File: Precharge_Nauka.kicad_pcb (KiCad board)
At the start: 4 copper layers, 100.8 x 101.4 mm, 238 parts, among them J1 Conn_02x02_Top_Bottom, J2 Conn_01x01, J3 Conn_01x01, J4 Conn_01x01, Q1 2N7002, Q2 C2M0280120D, Q3 C2M0280120D, Q4 C2M0280120D, Q5 C2M0280120D, U1 LM2903, U2 LMV321IDBVR, U3 74LVC1G08, U4 LMV321IDBVR

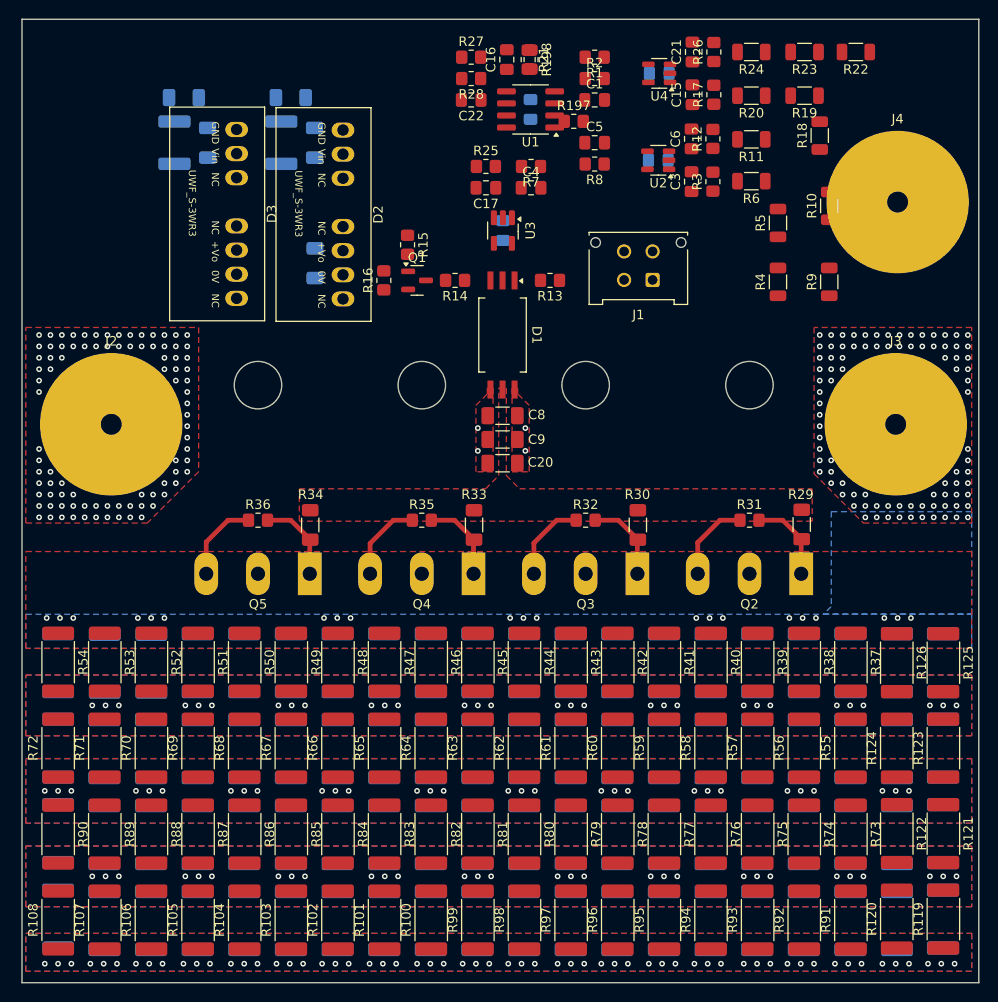
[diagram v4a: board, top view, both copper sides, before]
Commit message: VER1.0: увеличил фильтры компаратора, изменил схему предзарядных резисторов
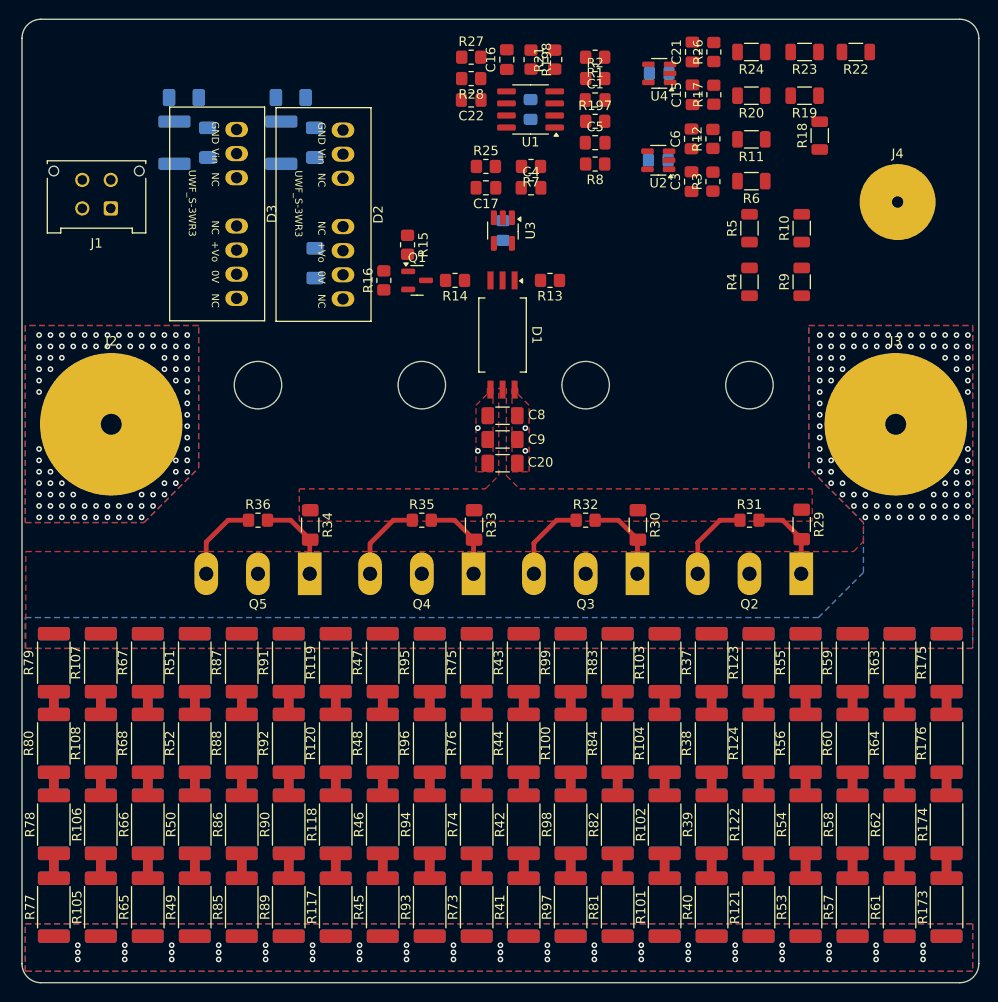
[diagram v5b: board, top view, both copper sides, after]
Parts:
- C16, C17, C4, C5: value 100n -> 1u
- J4: footprint Connector_Power:SMD_15mm -> Connector_Power:SMD_8mm
- R100, R101, R102, R103, R104, R105, R106, R107, R108, R109, R110, R111, R112, R113, R114, R115, R116, R119, R120, R121, R122, R123, R124, R127, R128, R129, R130, R131, R132, R133, R134, R135, R136, R137, R138, R139, R140, R141, R142, R143, R144, R145, R146, R147, R148, R149, R150, R151, R152, R153, R154, R155, R156, R157, R158, R159, R160, R161, R162, R163, R164, R165, R166, R167, R168, R169, R170, R171, R172, R177, R178, R179, R180, R181, R182, R183, R184, R185, R186, R187, R188, R189, R190, R191, R192, R193, R194, R195, R196, R37, R38, R39, R40, R41, R42, R43, R44, R45, R46, R47, R48, R49, R50, R51, R52, R53, R54, R55, R56, R57, R58, R59, R60, R61, R62, R63, R64, R65, R66, R67, R68, R73, R74, R75, R76, R77, R78, R79, R80, R81, R82, R83, R84, R85, R86, R87, R88, R89, R90, R91, R92, R93, R94, R95, R96, R97, R98, R99: value 15 -> 8.2k
- R117, R118, R173, R174, R175, R176: value 15 -> 8.2k; moved to F.Cu
- R125, R126, R69, R70, R71, R72: value 15 -> 8.2k; moved to B.Cu
- R197, R198: value 10k -> 100k
- R21, R8: value 120 -> 1k
- R25, R7: value 120 -> 10k
- U1: value LM2903 -> TS3702IDT
- moved R163 89.2 mm to (138.8, 189.5)
- moved R72 88.6 mm to (227.8, 198.0)
- moved R181 87.7 mm to (143.7, 215.2)
- moved R71 84.2 mm to (227.8, 189.5)
- moved R164 83.9 mm to (138.8, 198.0)
- moved R144 81.0 mm to (222.9, 198.0)
- moved R115 80.7 mm to (217.9, 189.5), turned to 90 degrees
- moved R182 80.7 mm to (143.7, 206.5)
- moved R54 80.5 mm to (217.9, 206.6)
- moved R113 80.5 mm to (217.9, 215.2), turned to -90 degrees
- moved R145 79.3 mm to (148.6, 215.2)
- moved R70 79.2 mm to (227.8, 206.5), turned to -90 degrees
- moved R143 78.7 mm to (222.9, 189.5)
- moved R53 78.2 mm to (217.9, 215.2)
- moved R69 75.7 mm to (227.8, 215.2), turned to -90 degrees
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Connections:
- R100 pad 1: VDC_OUT -> Net-(R100-Pad1)
- R100 pad 2: VDC_IN -> Net-(R100-Pad2)
- R101 pad 1: VDC_OUT -> Net-(R101-Pad1)
- R102 pad 1: VDC_OUT -> Net-(R102-Pad1)
- R102 pad 2: VDC_IN -> Net-(R101-Pad1)
- R103 pad 1: VDC_OUT -> Net-(R103-Pad1)
- R103 pad 2: VDC_IN -> VDC_OUT
- R104 pad 1: VDC_OUT -> Net-(R102-Pad1)
- R104 pad 2: VDC_IN -> Net-(R103-Pad1)
- R105 pad 1: VDC_OUT -> Net-(R105-Pad1)
- R106 pad 1: VDC_OUT -> Net-(R106-Pad1)
- R106 pad 2: VDC_IN -> Net-(R105-Pad1)
- R107 pad 1: VDC_OUT -> Net-(R107-Pad1)
- R107 pad 2: VDC_IN -> VDC_OUT
- R108 pad 1: VDC_OUT -> Net-(R106-Pad1)
- R108 pad 2: VDC_IN -> Net-(R107-Pad1)
- R109 pad 1: VDC_OUT -> Net-(R109-Pad1)
- R110 pad 1: VDC_OUT -> Net-(R110-Pad1)
- R110 pad 2: VDC_IN -> Net-(R109-Pad1)
- R111 pad 1: VDC_OUT -> Net-(R111-Pad1)
- R111 pad 2: VDC_IN -> VDC_OUT
- R112 pad 1: VDC_OUT -> Net-(R110-Pad1)
- R112 pad 2: VDC_IN -> Net-(R111-Pad1)
- R113 pad 1: VDC_OUT -> Net-(R113-Pad1)
- R114 pad 1: VDC_OUT -> Net-(R114-Pad1)
- R114 pad 2: VDC_IN -> Net-(R113-Pad1)
- R115 pad 1: VDC_OUT -> Net-(R115-Pad1)
- R115 pad 2: VDC_IN -> VDC_OUT
- R116 pad 1: VDC_OUT -> Net-(R114-Pad1)
- R116 pad 2: VDC_IN -> Net-(R115-Pad1)
- R117 pad 1: VDC_OUT -> Net-(R117-Pad1)
- R118 pad 1: VDC_OUT -> Net-(R118-Pad1)
- R118 pad 2: VDC_IN -> Net-(R117-Pad1)
- R119 pad 1: VDC_OUT -> Net-(R119-Pad1)
- R119 pad 2: VDC_IN -> VDC_OUT
- R120 pad 1: VDC_OUT -> Net-(R118-Pad1)
- R120 pad 2: VDC_IN -> Net-(R119-Pad1)
- R121 pad 1: VDC_OUT -> Net-(R121-Pad1)
- R122 pad 1: VDC_OUT -> Net-(R122-Pad1)
- R122 pad 2: VDC_IN -> Net-(R121-Pad1)
- R123 pad 1: VDC_OUT -> Net-(R123-Pad1)
- R123 pad 2: VDC_IN -> VDC_OUT
- R124 pad 1: VDC_OUT -> Net-(R122-Pad1)
- R124 pad 2: VDC_IN -> Net-(R123-Pad1)
- R125 pad 1: VDC_OUT -> Net-(R125-Pad1)
- R126 pad 1: VDC_OUT -> Net-(R126-Pad1)
- R126 pad 2: VDC_IN -> Net-(R125-Pad1)
- R127 pad 1: VDC_OUT -> Net-(R127-Pad1)
- R127 pad 2: VDC_IN -> VDC_OUT
- R128 pad 1: VDC_OUT -> Net-(R126-Pad1)
- R128 pad 2: VDC_IN -> Net-(R127-Pad1)
- R129 pad 1: VDC_OUT -> Net-(R129-Pad1)
- R130 pad 1: VDC_OUT -> Net-(R130-Pad1)
- R130 pad 2: VDC_IN -> Net-(R129-Pad1)
- R131 pad 1: VDC_OUT -> Net-(R131-Pad1)
- R131 pad 2: VDC_IN -> VDC_OUT
- R132 pad 1: VDC_OUT -> Net-(R130-Pad1)
- R132 pad 2: VDC_IN -> Net-(R131-Pad1)
- R133 pad 1: VDC_OUT -> Net-(R133-Pad1)
- R134 pad 1: VDC_OUT -> Net-(R134-Pad1)
- R134 pad 2: VDC_IN -> Net-(R133-Pad1)
- R135 pad 1: VDC_OUT -> Net-(R135-Pad1)
- R135 pad 2: VDC_IN -> VDC_OUT
- R136 pad 1: VDC_OUT -> Net-(R134-Pad1)
- R136 pad 2: VDC_IN -> Net-(R135-Pad1)
- R137 pad 1: VDC_OUT -> Net-(R137-Pad1)
- R138 pad 1: VDC_OUT -> Net-(R138-Pad1)
- R138 pad 2: VDC_IN -> Net-(R137-Pad1)
- R139 pad 1: VDC_OUT -> Net-(R139-Pad1)
- R139 pad 2: VDC_IN -> VDC_OUT
- R140 pad 1: VDC_OUT -> Net-(R138-Pad1)
- R140 pad 2: VDC_IN -> Net-(R139-Pad1)
- R141 pad 1: VDC_OUT -> Net-(R141-Pad1)
- R142 pad 1: VDC_OUT -> Net-(R142-Pad1)
- R142 pad 2: VDC_IN -> Net-(R141-Pad1)
- R143 pad 1: VDC_OUT -> Net-(R143-Pad1)
- R143 pad 2: VDC_IN -> VDC_OUT
- R144 pad 1: VDC_OUT -> Net-(R142-Pad1)
- R144 pad 2: VDC_IN -> Net-(R143-Pad1)
- R145 pad 1: VDC_OUT -> Net-(R145-Pad1)
- R146 pad 1: VDC_OUT -> Net-(R146-Pad1)
- R146 pad 2: VDC_IN -> Net-(R145-Pad1)
- R147 pad 1: VDC_OUT -> Net-(R147-Pad1)
- R147 pad 2: VDC_IN -> VDC_OUT
- R148 pad 1: VDC_OUT -> Net-(R146-Pad1)
- R148 pad 2: VDC_IN -> Net-(R147-Pad1)
- R149 pad 1: VDC_OUT -> Net-(R149-Pad1)
- R150 pad 1: VDC_OUT -> Net-(R150-Pad1)
- R150 pad 2: VDC_IN -> Net-(R149-Pad1)
- R151 pad 1: VDC_OUT -> Net-(R151-Pad1)
- R151 pad 2: VDC_IN -> VDC_OUT
- R152 pad 1: VDC_OUT -> Net-(R150-Pad1)
- R152 pad 2: VDC_IN -> Net-(R151-Pad1)
- R153 pad 1: VDC_OUT -> Net-(R153-Pad1)
- R154 pad 1: VDC_OUT -> Net-(R154-Pad1)
- R154 pad 2: VDC_IN -> Net-(R153-Pad1)
- R155 pad 1: VDC_OUT -> Net-(R155-Pad1)
- R155 pad 2: VDC_IN -> VDC_OUT
- R156 pad 1: VDC_OUT -> Net-(R154-Pad1)
- R156 pad 2: VDC_IN -> Net-(R155-Pad1)
- R157 pad 1: VDC_OUT -> Net-(R157-Pad1)
- R158 pad 1: VDC_OUT -> Net-(R158-Pad1)
- R158 pad 2: VDC_IN -> Net-(R157-Pad1)
- R159 pad 1: VDC_OUT -> Net-(R159-Pad1)
- R159 pad 2: VDC_IN -> VDC_OUT
- R160 pad 1: VDC_OUT -> Net-(R158-Pad1)
- R160 pad 2: VDC_IN -> Net-(R159-Pad1)
- R161 pad 1: VDC_OUT -> Net-(R161-Pad1)
- R162 pad 1: VDC_OUT -> Net-(R162-Pad1)
- R162 pad 2: VDC_IN -> Net-(R161-Pad1)
- R163 pad 1: VDC_OUT -> Net-(R163-Pad1)
- R163 pad 2: VDC_IN -> VDC_OUT
- R164 pad 1: VDC_OUT -> Net-(R162-Pad1)
- R164 pad 2: VDC_IN -> Net-(R163-Pad1)
- R165 pad 1: VDC_OUT -> Net-(R165-Pad1)
- R166 pad 1: VDC_OUT -> Net-(R166-Pad1)
- R166 pad 2: VDC_IN -> Net-(R165-Pad1)
- R167 pad 1: VDC_OUT -> Net-(R167-Pad1)
- R167 pad 2: VDC_IN -> VDC_OUT
- R168 pad 1: VDC_OUT -> Net-(R166-Pad1)
- R168 pad 2: VDC_IN -> Net-(R167-Pad1)
- R169 pad 1: VDC_OUT -> Net-(R169-Pad1)
- R170 pad 1: VDC_OUT -> Net-(R170-Pad1)
- R170 pad 2: VDC_IN -> Net-(R169-Pad1)
- R171 pad 1: VDC_OUT -> Net-(R171-Pad1)
- R171 pad 2: VDC_IN -> VDC_OUT
- R172 pad 1: VDC_OUT -> Net-(R170-Pad1)
- R172 pad 2: VDC_IN -> Net-(R171-Pad1)
- R173 pad 1: VDC_OUT -> Net-(R173-Pad1)
- R174 pad 1: VDC_OUT -> Net-(R174-Pad1)
- R174 pad 2: VDC_IN -> Net-(R173-Pad1)
- R175 pad 1: VDC_OUT -> Net-(R175-Pad1)
- R175 pad 2: VDC_IN -> VDC_OUT
- R176 pad 1: VDC_OUT -> Net-(R174-Pad1)
- R176 pad 2: VDC_IN -> Net-(R175-Pad1)
- R177 pad 1: VDC_OUT -> Net-(R177-Pad1)
- R178 pad 1: VDC_OUT -> Net-(R178-Pad1)
- R178 pad 2: VDC_IN -> Net-(R177-Pad1)
- R179 pad 1: VDC_OUT -> Net-(R179-Pad1)
- R179 pad 2: VDC_IN -> VDC_OUT
- R180 pad 1: VDC_OUT -> Net-(R178-Pad1)
- R180 pad 2: VDC_IN -> Net-(R179-Pad1)
- R181 pad 1: VDC_OUT -> Net-(R181-Pad1)
- R182 pad 1: VDC_OUT -> Net-(R182-Pad1)
- R182 pad 2: VDC_IN -> Net-(R181-Pad1)
- R183 pad 1: VDC_OUT -> Net-(R183-Pad1)
- R183 pad 2: VDC_IN -> VDC_OUT
- R184 pad 1: VDC_OUT -> Net-(R182-Pad1)
- R184 pad 2: VDC_IN -> Net-(R183-Pad1)
- R185 pad 1: VDC_OUT -> Net-(R185-Pad1)
- R186 pad 1: VDC_OUT -> Net-(R186-Pad1)
- R186 pad 2: VDC_IN -> Net-(R185-Pad1)
- R187 pad 1: VDC_OUT -> Net-(R187-Pad1)
- R187 pad 2: VDC_IN -> VDC_OUT
- R188 pad 1: VDC_OUT -> Net-(R186-Pad1)
- R188 pad 2: VDC_IN -> Net-(R187-Pad1)
- R189 pad 1: VDC_OUT -> Net-(R189-Pad1)
- R190 pad 1: VDC_OUT -> Net-(R190-Pad1)
- R190 pad 2: VDC_IN -> Net-(R189-Pad1)
- R191 pad 1: VDC_OUT -> Net-(R191-Pad1)
- R191 pad 2: VDC_IN -> VDC_OUT
- R192 pad 1: VDC_OUT -> Net-(R190-Pad1)
- R192 pad 2: VDC_IN -> Net-(R191-Pad1)
- R193 pad 1: VDC_OUT -> Net-(R193-Pad1)
- R194 pad 1: VDC_OUT -> Net-(R194-Pad1)
- R194 pad 2: VDC_IN -> Net-(R193-Pad1)
- R195 pad 1: VDC_OUT -> Net-(R195-Pad1)
- R195 pad 2: VDC_IN -> VDC_OUT
- R196 pad 1: VDC_OUT -> Net-(R194-Pad1)
- R196 pad 2: VDC_IN -> Net-(R195-Pad1)
- R37 pad 1: VDC_OUT -> Net-(R37-Pad1)
- R37 pad 2: VDC_IN -> VDC_OUT
- R38 pad 1: VDC_OUT -> Net-(R38-Pad1)
- R38 pad 2: VDC_IN -> Net-(R37-Pad1)
- R39 pad 1: VDC_OUT -> Net-(R38-Pad1)
- R39 pad 2: VDC_IN -> Net-(R39-Pad2)
- R40 pad 1: VDC_OUT -> Net-(R39-Pad2)
- R41 pad 1: VDC_OUT -> Net-(R41-Pad1)
- R42 pad 1: VDC_OUT -> Net-(R42-Pad1)
- R42 pad 2: VDC_IN -> Net-(R41-Pad1)
- R43 pad 1: VDC_OUT -> Net-(R43-Pad1)
- R43 pad 2: VDC_IN -> VDC_OUT
- R44 pad 1: VDC_OUT -> Net-(R42-Pad1)
- R44 pad 2: VDC_IN -> Net-(R43-Pad1)
- R45 pad 1: VDC_OUT -> Net-(R45-Pad1)
- R46 pad 1: VDC_OUT -> Net-(R46-Pad1)
- R46 pad 2: VDC_IN -> Net-(R45-Pad1)
- R47 pad 1: VDC_OUT -> Net-(R47-Pad1)
- R47 pad 2: VDC_IN -> VDC_OUT
- R48 pad 1: VDC_OUT -> Net-(R46-Pad1)
- R48 pad 2: VDC_IN -> Net-(R47-Pad1)
- R49 pad 1: VDC_OUT -> Net-(R49-Pad1)
- R50 pad 1: VDC_OUT -> Net-(R50-Pad1)
- R50 pad 2: VDC_IN -> Net-(R49-Pad1)
- R51 pad 1: VDC_OUT -> Net-(R51-Pad1)
- R51 pad 2: VDC_IN -> VDC_OUT
- R52 pad 1: VDC_OUT -> Net-(R50-Pad1)
- R52 pad 2: VDC_IN -> Net-(R51-Pad1)
- R53 pad 1: VDC_OUT -> Net-(R53-Pad1)
- R54 pad 1: VDC_OUT -> Net-(R54-Pad1)
- R54 pad 2: VDC_IN -> Net-(R53-Pad1)
- R55 pad 1: VDC_OUT -> Net-(R55-Pad1)
- R55 pad 2: VDC_IN -> VDC_OUT
- R56 pad 1: VDC_OUT -> Net-(R54-Pad1)
- R56 pad 2: VDC_IN -> Net-(R55-Pad1)
- R57 pad 1: VDC_OUT -> Net-(R57-Pad1)
- R58 pad 1: VDC_OUT -> Net-(R58-Pad1)
- R58 pad 2: VDC_IN -> Net-(R57-Pad1)
- R59 pad 1: VDC_OUT -> Net-(R59-Pad1)
- R59 pad 2: VDC_IN -> VDC_OUT
- R60 pad 1: VDC_OUT -> Net-(R58-Pad1)
- R60 pad 2: VDC_IN -> Net-(R59-Pad1)
- R61 pad 1: VDC_OUT -> Net-(R61-Pad1)
- R62 pad 1: VDC_OUT -> Net-(R62-Pad1)
- R62 pad 2: VDC_IN -> Net-(R61-Pad1)
- R63 pad 1: VDC_OUT -> Net-(R63-Pad1)
- R63 pad 2: VDC_IN -> VDC_OUT
- R64 pad 1: VDC_OUT -> Net-(R62-Pad1)
- R64 pad 2: VDC_IN -> Net-(R63-Pad1)
- R65 pad 1: VDC_OUT -> Net-(R65-Pad1)
- R66 pad 1: VDC_OUT -> Net-(R66-Pad1)
- R66 pad 2: VDC_IN -> Net-(R65-Pad1)
- R67 pad 1: VDC_OUT -> Net-(R67-Pad1)
- R67 pad 2: VDC_IN -> VDC_OUT
- R68 pad 1: VDC_OUT -> Net-(R66-Pad1)
- R68 pad 2: VDC_IN -> Net-(R67-Pad1)
- R69 pad 1: VDC_OUT -> Net-(R69-Pad1)
- R70 pad 1: VDC_OUT -> Net-(R70-Pad1)
- R70 pad 2: VDC_IN -> Net-(R69-Pad1)
- R71 pad 1: VDC_OUT -> Net-(R71-Pad1)
- R71 pad 2: VDC_IN -> VDC_OUT
- R72 pad 1: VDC_OUT -> Net-(R70-Pad1)
- R72 pad 2: VDC_IN -> Net-(R71-Pad1)
- R73 pad 1: VDC_OUT -> Net-(R73-Pad1)
- R74 pad 1: VDC_OUT -> Net-(R74-Pad1)
- R74 pad 2: VDC_IN -> Net-(R73-Pad1)
- R75 pad 1: VDC_OUT -> Net-(R75-Pad1)
- R75 pad 2: VDC_IN -> VDC_OUT
- R76 pad 1: VDC_OUT -> Net-(R74-Pad1)
- R76 pad 2: VDC_IN -> Net-(R75-Pad1)
- R77 pad 1: VDC_OUT -> Net-(R77-Pad1)
- R78 pad 1: VDC_OUT -> Net-(R78-Pad1)
- R78 pad 2: VDC_IN -> Net-(R77-Pad1)
- R79 pad 1: VDC_OUT -> Net-(R79-Pad1)
- R79 pad 2: VDC_IN -> VDC_OUT
- R80 pad 1: VDC_OUT -> Net-(R78-Pad1)
- R80 pad 2: VDC_IN -> Net-(R79-Pad1)
- R81 pad 1: VDC_OUT -> Net-(R81-Pad1)
- R82 pad 1: VDC_OUT -> Net-(R82-Pad1)
- R82 pad 2: VDC_IN -> Net-(R81-Pad1)
- R83 pad 1: VDC_OUT -> Net-(R83-Pad1)
- R83 pad 2: VDC_IN -> VDC_OUT
- R84 pad 1: VDC_OUT -> Net-(R82-Pad1)
- R84 pad 2: VDC_IN -> Net-(R83-Pad1)
- R85 pad 1: VDC_OUT -> Net-(R85-Pad1)
- R86 pad 1: VDC_OUT -> Net-(R86-Pad1)
- R86 pad 2: VDC_IN -> Net-(R85-Pad1)
- R87 pad 1: VDC_OUT -> Net-(R87-Pad1)
- R87 pad 2: VDC_IN -> VDC_OUT
- R88 pad 1: VDC_OUT -> Net-(R86-Pad1)
- R88 pad 2: VDC_IN -> Net-(R87-Pad1)
- R89 pad 1: VDC_OUT -> Net-(R89-Pad1)
- R90 pad 1: VDC_OUT -> Net-(R90-Pad1)
- R90 pad 2: VDC_IN -> Net-(R89-Pad1)
- R91 pad 1: VDC_OUT -> Net-(R91-Pad1)
- R91 pad 2: VDC_IN -> VDC_OUT
- R92 pad 1: VDC_OUT -> Net-(R90-Pad1)
- R92 pad 2: VDC_IN -> Net-(R91-Pad1)
- R93 pad 1: VDC_OUT -> Net-(R93-Pad1)
- R94 pad 1: VDC_OUT -> Net-(R94-Pad1)
- R94 pad 2: VDC_IN -> Net-(R93-Pad1)
- R95 pad 1: VDC_OUT -> Net-(R95-Pad1)
- R95 pad 2: VDC_IN -> VDC_OUT
- R96 pad 1: VDC_OUT -> Net-(R94-Pad1)
- R96 pad 2: VDC_IN -> Net-(R95-Pad1)
- R97 pad 1: VDC_OUT -> Net-(R97-Pad1)
- R98 pad 1: VDC_OUT -> Net-(R100-Pad1)
- R98 pad 2: VDC_IN -> Net-(R97-Pad1)
- R99 pad 1: VDC_OUT -> Net-(R100-Pad2)
- R99 pad 2: VDC_IN -> VDC_OUT
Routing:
- net Net-(R69-Pad1): track 0.00 -> 2.65 mm
- net Net-(R193-Pad1): track 0.00 -> 2.65 mm
- net Net-(R189-Pad1): track 0.00 -> 2.65 mm
- net Net-(R185-Pad1): track 0.00 -> 2.65 mm
- net Net-(R181-Pad1): track 0.00 -> 2.65 mm
- net Net-(R177-Pad1): track 0.00 -> 2.65 mm
- net Net-(R169-Pad1): track 0.00 -> 2.65 mm
- net Net-(R165-Pad1): track 0.00 -> 2.65 mm
- net Net-(R161-Pad1): track 0.00 -> 2.65 mm
- net Net-(R157-Pad1): track 0.00 -> 2.65 mm
- net Net-(R153-Pad1): track 0.00 -> 2.65 mm
- net Net-(R149-Pad1): track 0.00 -> 2.65 mm
- net Net-(R145-Pad1): track 0.00 -> 2.65 mm
- net Net-(R141-Pad1): track 0.00 -> 2.65 mm
- net Net-(R137-Pad1): track 0.00 -> 2.65 mm
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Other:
- outline, holes or cut-outs redrawn

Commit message: VER1.0: изменил контур платы, сложно скомпоновать в размер
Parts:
- removed C8: 0.1u, Capacitor_SMD:C_1206_3216Metric_Pad1.33x1.80mm_HandSolder
- added Q6: 2N7002, Package_TO_SOT_SMD:SOT-23, F.Cu at (140.5, 148.8)
- added R199: 250, Resistor_SMD:R_0805_2012Metric_Pad1.20x1.40mm_HandSolder, F.Cu at (138.5, 151.8)
- added R200: 250, Resistor_SMD:R_0805_2012Metric_Pad1.20x1.40mm_HandSolder, F.Cu at (138.5, 145.8)
- added R201: 1, Resistor_SMD:R_0805_2012Metric_Pad1.20x1.40mm_HandSolder, F.Cu at (144.5, 147.5)
- added R202: 10k, Resistor_SMD:R_0805_2012Metric_Pad1.20x1.40mm_HandSolder, F.Cu at (137.5, 148.8)
- added R203: 10k, Resistor_SMD:R_0805_2012Metric_Pad1.20x1.40mm_HandSolder, F.Cu at (144.2, 151.5)
- added U5: PC817, Package_DIP:DIP-4_W7.62mm, F.Cu at (135.1, 150.0)
- C17, C4, R25, R7: moved to B.Cu
- J1: value Conn_02x02_Top_Bottom -> Conn_02x03_Top_Bottom; footprint Connector_Molex:Molex_Micro-Fit_3.0_43045-0412_2x02_P3.00mm_Vertical -> Connector_Molex:Molex_Micro-Fit_3.0_43045-0612_2x03_P3.00mm_Vertical
- moved J4 67.8 mm to (160.2, 148.8)
- moved C11 63.3 mm to (114.2, 169.5)
- moved C12 63.3 mm to (116.8, 174.2)
- moved D2 63.3 mm to (119.8, 181.8)
- moved L1 63.3 mm to (113.2, 174.2)
- moved C13 63.1 mm to (117.1, 186.9)
- moved R18 60.6 mm to (167.8, 165.8), turned to 0 degrees
- moved R22 60.3 mm to (177.5, 164.5), turned to 0 degrees
- moved R19 57.1 mm to (170.5, 161.8), turned to 90 degrees
- moved R23 50.3 mm to (178.2, 156.2)
- moved R24 49.4 mm to (173.8, 156.2), turned to 90 degrees
- moved R20 49.4 mm to (170.5, 156.2), turned to 90 degrees
- moved C18 47.5 mm to (126.2, 169.6)
- moved L2 47.5 mm to (125.2, 174.3)
- moved C19 47.5 mm to (128.7, 174.3)
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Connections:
- J1 pad 3: +27V -> Ready
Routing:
- net Net-(R198-Pad2): track 0.00 -> 43.7 mm, vias 0 -> 1
- net Net-(U1A-+): track 0.00 -> 26.4 mm
- net GND1: track 0.00 -> 24.8 mm, vias 0 -> 11
- net Net-(R197-Pad2): track 0.00 -> 23.9 mm, vias 0 -> 1
- net GNDPWR: track 0.00 -> 22.3 mm, vias 0 -> 1
- net VCC: track 46.4 -> 65.4 mm, vias 2 -> 1
- net Net-(U1B--): track 0.00 -> 14.9 mm
- net +5V: track 0.00 -> 13.6 mm, vias 0 -> 7
- net Net-(U1B-+): track 0.00 -> 13.0 mm
- net Net-(C6-Pad2): track 0.00 -> 12.2 mm
- net Net-(C21-Pad2): track 0.00 -> 9.70 mm, vias 0 -> 1
- net Net-(R22-Pad2): track 0.00 -> 9.63 mm
- net Net-(Q1-G): track 0.00 -> 7.96 mm
- net Net-(C17-Pad1): track 0.00 -> 7.62 mm, vias 0 -> 1
- net Net-(U2--): track 0.00 -> 7.45 mm
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- added copper zone on In2.Cu, net +5V
- added copper zone on In1.Cu, net GND1
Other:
- board size 100.8 x 101.4 mm -> 125.8 x 79.4 mm

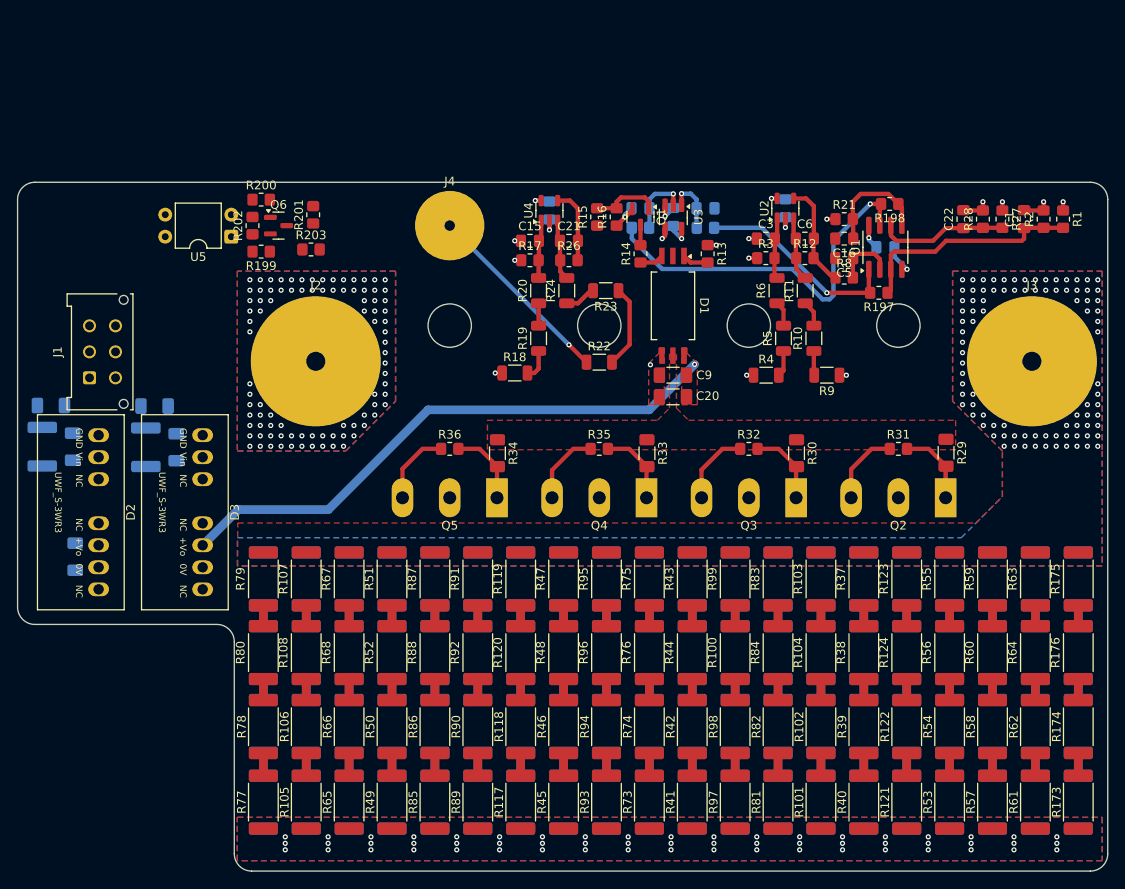
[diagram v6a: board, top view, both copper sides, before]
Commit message: VER1.0: уместил в прямоугольник все, заменил операционники измерительные
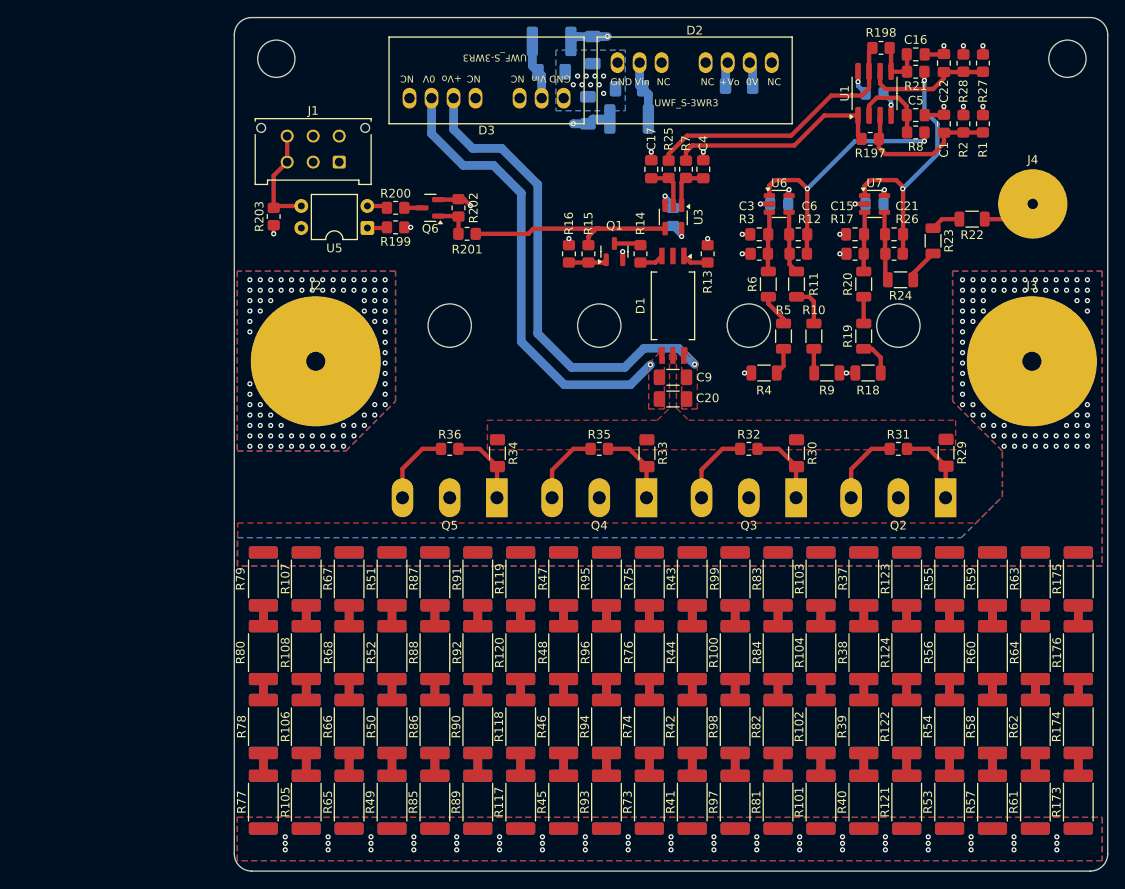
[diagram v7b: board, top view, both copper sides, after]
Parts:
- removed U2, U4: LMV321IDBVR, Package_TO_SOT_SMD:SOT-23-5
- added H1: MountingHole, MountingHole:MountingHole_4.3mm_M4, F.Cu at (140.2, 129.5)
- added H2: MountingHole, MountingHole:MountingHole_4.3mm_M4, F.Cu at (231.5, 129.5)
- added U6: OPA333xxDBV, Package_TO_SOT_SMD:SOT-23-5, F.Cu at (198.2, 146.2)
- added U7: OPA333xxDBV, Package_TO_SOT_SMD:SOT-23-5, F.Cu at (209.2, 146.2)
- C17, C4, R25, R7: moved to F.Cu
- moved C13 93.9 mm to (193.6, 132.6), turned to 180 degrees
- moved D2 86.1 mm to (188.5, 129.9), turned to 0 degrees
- moved L1 77.5 mm to (180.9, 136.4), turned to 180 degrees
- moved C12 76.3 mm to (180.9, 132.9), turned to 180 degrees
- moved C11 70.7 mm to (176.2, 135.4), turned to 90 degrees
- moved J4 67.3 mm to (227.5, 146.2)
- moved L2 66.2 mm to (172.0, 127.5), turned to 0 degrees
- moved C18 65.1 mm to (176.8, 128.5), turned to -90 degrees
- moved C19 61.2 mm to (172.0, 131.0), turned to 0 degrees
- moved D3 57.9 mm to (164.5, 134.1), turned to 180 degrees
- moved R22 46.1 mm to (220.5, 148.0), turned to 180 degrees
- moved R18 40.8 mm to (208.5, 165.8)
- moved R24 38.5 mm to (212.2, 155.0), turned to 180 degrees
- moved R23 38.2 mm to (216.0, 150.5), turned to -90 degrees
- moved J1 38.1 mm to (147.5, 141.4), turned to 180 degrees
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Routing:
- net VDC_OUT: track 41.0 -> 89.0 mm, vias 93 -> 78
- net Shunt_ON: track 1.29 -> 24.7 mm, vias 1 -> 0
- net Net-(C21-Pad2): track 9.70 -> 29.7 mm, vias 1 -> 2
- net Net-(C6-Pad2): track 12.2 -> 30.5 mm, vias 0 -> 2
- net GNDPWR: track 22.3 -> 6.26 mm, vias 1 -> 0
- net Ready: track 0.00 -> 12.2 mm
- net Net-(R198-Pad2): track 43.7 -> 31.8 mm, vias 1 -> 0
- net VCC: track 65.4 -> 54.5 mm
- net +27V: track 0.00 -> 8.90 mm, vias 0 -> 2
- net Net-(U1A-+): track 26.4 -> 17.8 mm
- net GND1: track 24.8 -> 32.4 mm, vias 11 -> 17
- net Net-(D3-Vin): track 0.00 -> 7.00 mm
- net Net-(D2-Vin): track 0.00 -> 6.92 mm
- net Net-(U1B-+): track 13.0 -> 6.62 mm
- net Net-(R22-Pad2): track 9.63 -> 3.47 mm
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- added copper zone on In2.Cu, net +27V
- added copper zone on In1.Cu, net +5V
- added copper zone on B.Cu, net GND
- added copper zone on In1.Cu, net GND
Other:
- board size 125.8 x 79.4 mm -> 100.8 x 98.4 mm
